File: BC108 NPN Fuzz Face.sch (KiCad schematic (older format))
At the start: 20 parts, among them J1 Jack-DC, Q1 BC108, Q2 BC108

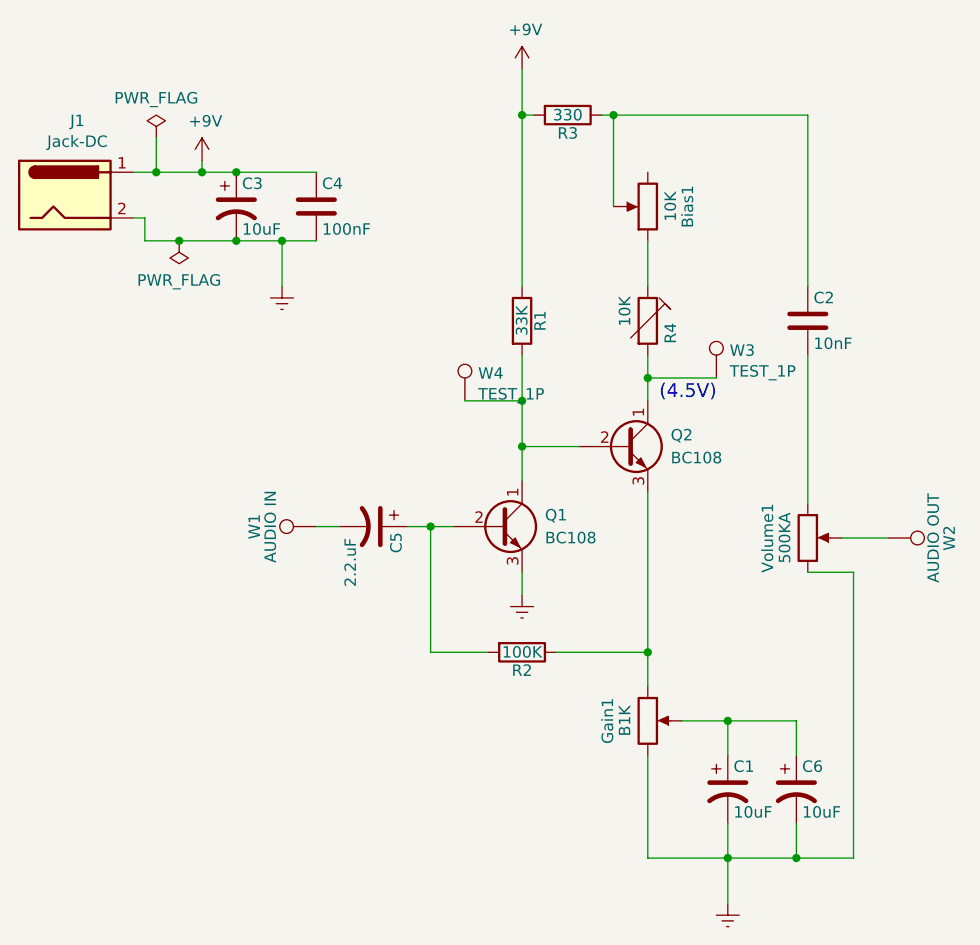
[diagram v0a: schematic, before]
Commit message: Some corrections after first PCB
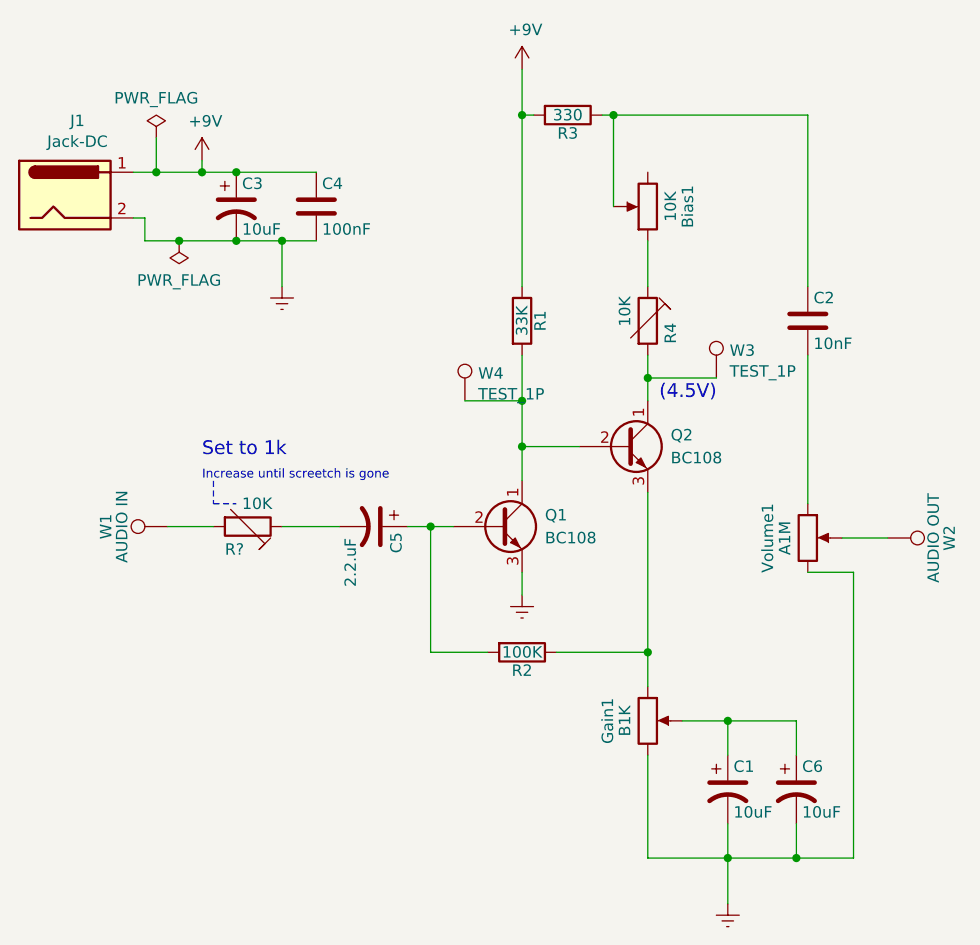
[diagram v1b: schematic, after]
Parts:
- added R?: 10K, Potentiometer_THT:Potentiometer_Bourns_3266Z_Horizontal, symbol BC108-NPN-Fuzz-Face-rescue:RTRIM
- Volume1: value 500KA -> A1M
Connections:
- net at W1.1: now also R?.2; no longer C5.2
- new net: C5.2, R?.1
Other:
- note added: "Increase until screetch is gone"
- note added: "Set to 1k"
- moved on the sheet: W1
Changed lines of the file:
@@
 L BC108-NPN-Fuzz-Face-rescue:TEST_1P W1
 U 1 1 5F64E9AA
-P 5100 4450
-F 0 "W1" H 5100 4720 50  0000 C CNN
-F 1 "AUDIO IN" H 5100 4650 50  0000 C CNN
-F 2 "Connector_PinHeader_2.54mm:PinHeader_1x01_P2.54mm_Vertical" H 5300 4450 50  0001 C CNN
-F 3 "" H 5300 4450 50  0000 C CNN
-	1    5100 4450
+P 4450 4450
+F 0 "W1" H 4450 4720 50  0000 C CNN
+F 1 "AUDIO IN" H 4450 4650 50  0000 C CNN
+F 2 "Connector_PinHeader_2.54mm:PinHeader_1x01_P2.54mm_Vertical" H 4650 4450 50  0001 C CNN
+F 3 "" H 4650 4450 50  0000 C CNN
+	1    4450 4450
 	0    -1   -1   0
 $EndComp
@@
 Connection ~ 5600 4450
 Wire Wire Line
-	5100 4450 5200 4450
-Wire Wire Line
 	6000 4100 6250 4100
 Wire Wire Line
@@
 P 7250 4500
 F 0 "Volume1" V 7075 4500 50  0000 C CNN
-F 1 "500KA" V 7150 4500 50  0000 C CNN
+F 1 "A1M" V 7150 4500 50  0000 C CNN
 F 2 "Connector_Wire:SolderWirePad_1x03_P3.175mm_Drill0.8mm" H 7250 4500 50  0001 C CNN
 F 3 "" H 7250 4500 50  0000 C CNN
@@
 	6000 2450 6000 2650
 Connection ~ 6000 2650
+$Comp
+L BC108-NPN-Fuzz-Face-rescue:RTRIM R?
+U 1 1 5F958E26
+P 4800 4450
+F 0 "R?" V 4900 4350 50  0000 L CNN
+F 1 "10K" V 4700 4425 50  0000 L CNN
+F 2 "Potentiometer_THT:Potentiometer_Bourns_3266Z_Horizontal" V 4730 4450 50  0001 C CNN
+F 3 "" H 4800 4450 50  0000 C CNN
+	1    4800 4450
+	0    1    1    0
+$EndComp
+Wire Wire Line
+	4450 4450 4650 4450
+Wire Wire Line
+	4950 4450 5200 4450
+Text Notes 4600 4150 0    60   ~ 0
+Set to 1k
+Text Notes 4600 4250 0    39   ~ 0
+Increase until screetch is gone
+Wire Notes Line
+	4650 4250 4650 4350
+Wire Notes Line
+	4650 4350 4750 4350
 $EndSCHEMATC
